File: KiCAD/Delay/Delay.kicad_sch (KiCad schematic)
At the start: 65 parts, among them J1 IN, J2 OUT, J3 Conn_01x03, J4 Conn_01x03, U1 TL072, U2 TL072, U3 PT2399, U4 L7805

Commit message: Delay PCB
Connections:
- net DELAY: now also R3.1; no longer R3.2
- net at C2.1, R6.2, U1.1: now also R8.2; no longer R8.1
- net at C3.2, R4.1, U1.6 (-): now also R2.1, R3.2; no longer R2.2, R3.1
- net at D1.2 (A), D3.1 (K), R9.1: now also R8.1; no longer R8.2
- net at C1.1, R1.1: now also R2.2; no longer R2.1
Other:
- moved on the sheet: R2, R3, R8
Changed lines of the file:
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@@
 	(symbol
 		(lib_id "HackSynth:R")
-		(at 62.23 78.74 90)
+		(at 62.23 78.74 270)
 		(unit 1)
 		(exclude_from_sim no)
@@
 		)
 		(property "Footprint" "HackSynth:R_Vertical_P2.54mm"
-			(at 62.23 80.518 90)
+			(at 62.23 76.962 90)
 			(effects
 				(font
@@
 	(symbol
 		(lib_id "HackSynth:R")
-		(at 81.28 49.53 90)
+		(at 81.28 49.53 270)
 		(unit 1)
 		(exclude_from_sim no)
@@
 		)
 		(property "Footprint" "HackSynth:R_Vertical_P2.54mm"
-			(at 81.28 51.308 90)
+			(at 81.28 47.752 90)
 			(effects
 				(font
@@
 	(symbol
 		(lib_id "HackSynth:R")
-		(at 43.18 99.06 90)
+		(at 43.18 99.06 270)
 		(unit 1)
 		(exclude_from_sim no)
@@
 		(dnp no)
 		(property "Reference" "R2"
-			(at 43.18 97.028 90)
+			(at 43.18 96.774 90)
 			(effects
 				(font
@@
 		)
 		(property "Footprint" "HackSynth:R_Vertical_P2.54mm"
-			(at 43.18 100.838 90)
+			(at 43.18 97.282 90)
 			(effects
 				(font

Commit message: Delay PCB
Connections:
- net at C21.2, R19.2, R23.2: now also R18.1; no longer R18.2
- net at C17.1, U3.16 (LPF1-IN): now also R18.2; no longer R18.1
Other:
- moved on the sheet: R18
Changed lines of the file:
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@@
 			"gtJqHJTWHJSWgtJqHJTWHJSWgtJqHJTWHJSWgtJqHJTWHJSWIpK2hxHREqNQWjNQWoq1tJcDEW2x"
 			"j38zCAGlpVhLiyAaBqWloLSIF/HOJ7z9UadpjtIi3kM6v9Ov2xhL/v/mElWvvu6fRQAAAABJRU5E"
-			"rkJggg=="
+			"rkJgggAgACAAIAAgACAAIAAgAD0AIAAiAHMAdABhAHQAaQBjAHQAZQB4AHQAIgANAA0ACgAvAD4A"
+			"DQANAAoAPAAvAGkAZgA+AA0ADQAKADwAaQBmACAAaQBkAD0AIgBhAHQAbwBtACgARgBvAG8AdABu"
+			"AG8AdABlAFQAZQB4AHQATABpAG4AawApACIAPgANAA0ACgA8AGMAYwBzAHkAcwBsAGkAbgBrAA0A"
+			"DQAKAGYAbwBuAHQAIAAgACAAIAAgACAAIAAgACAAIAAgACAAIAAgACAAIAA9ACAAIgBnAHQAZgAo"
+			"AFQAYQBzAGsARABpAGEAbABvAGcAUwB0AHkAbABlACwAIAAxADUALAAgADAAKQAiAA0ADQAKAGYA"
+			"bwByAGUAZwByAG8AdQBuAGQAIAAgACAAIAAgACAAIAAgACAAIAA9ACAAIgBnAHQAYwAoAFQAYQBz"
+			"AGsARABpAGEAbABvAGcAUwB0AHkAbABlACwAIAAxADUALAAgADAALAAgADMAOAAwADMAKQAiAA0A"
+			"DQAKAC8APgANAA0ACgA8AC8AaQBmAD4ADQANAAoAPABpAGYAIABpAGQAPQAiAGEAdABvAG0AKABF"
+			"AHgAcABhAG4AZABlAGQARgBvAG8AdABlAHIAQQByAGUAYQApACIAPgANAA0ACgA8AGUAbABlAG0A"
+			"ZQBuAHQADQANAAoAYgBhAGMAawBnAHIAbwB1AG4AZAAgACAAIAAgACAAIAAgACAAIAAgAD0AIAAi"
+			"AHQAaABlAG0AZQBhAGIAbABlACgAZAB0AGIAKABUAGEAcwBrAEQAaQBhAGwAbwBnACwAIAAxADUA"
+			"LAAgADAAKQAsACAAdABoAHIAZQBlAGQAZgBhAGMAZQApACIADQANAAoAcABhAGQAZABpAG4AZwAg"
+			"ACAAIAAgACAAIAAgACAAIAAgACAAIAAgAD0AIAAiAHQAaABlAG0AZQBhAGIAbABlACgAZwB0AG0A"
+			"YQByACgAVABhAHMAawBEAGkAYQBsAG8AZwAsACAAMQA4ACwAIAAwACwAIAAzADYAMAAyACkALABy"
+			"AGUAYwB0ACgAMQAwAHIAcAAsADAALAAxADAAcgBwACwANQByAHAAKQApACIADQANAAoALwA+AA0A"
+			"DQAKADwALwBpAGYAPgANAA0ACgA8AGkAZgAgAGkAZAA9ACIAYQB0AG8AbQAoAEUAeABwAGEAbgBk"
+			"AGUAZABGAG8AbwB0AGUAcgBUAGUAeAB0ACkAIgA+AA0ADQAKADwAZQBsAGUAbQBlAG4AdAANAA0A"
+			"CgBmAG8AbgB0ACAAIAAgACAAIAAgACAAIAAgACAAIAAgACAAIAAgACAAPQAgACIAZwB0AGYAKABU"
+			"AGEAcw=="
 		)
 	)
@@
 	(symbol
 		(lib_id "HackSynth:R")
-		(at 251.46 95.25 90)
+		(at 251.46 95.25 270)
 		(unit 1)
 		(exclude_from_sim no)
@@
 		)
 		(property "Footprint" "HackSynth:R_Vertical_P2.54mm"
-			(at 251.46 97.028 90)
+			(at 251.46 93.472 90)
 			(effects
 				(font

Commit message: Backup Cleanup
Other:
- moved on the sheet: C6, J3, J4, R24, R25, RV3

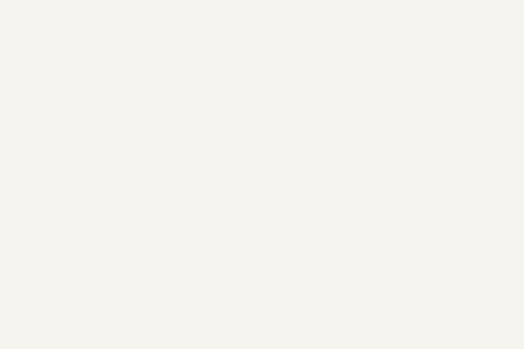
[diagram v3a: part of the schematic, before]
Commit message: Footprint Edits
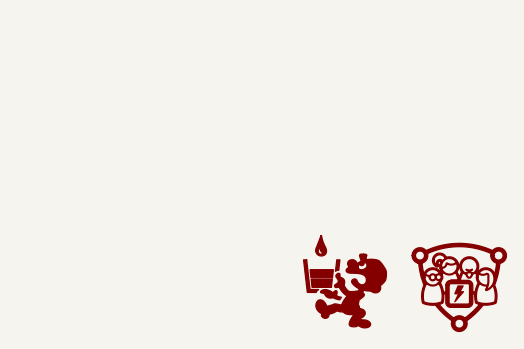
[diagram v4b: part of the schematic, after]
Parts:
- added G1: ~, symbol HackSynth:CCHS_Logo
- added G2: ~, symbol HackSynth:Logo_PancakeLegend
- C13: footprint HackSynth:CP_Radial_D5.2mm_P2.50mm_LayDown -> HackSynth:CP_Radial_D5.2mm_P2.50mm_LayDown_Mirror
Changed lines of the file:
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@@
 	)
 	(symbol
+		(lib_id "HackSynth:CCHS_Logo")
+		(at 275.59 172.72 0)
+		(unit 1)
+		(exclude_from_sim no)
+		(in_bom yes)
+		(on_board yes)
+		(dnp no)
+		(fields_autoplaced yes)
+		(property "Reference" "G1"
+			(at 275.59 180.34 0)
+			(effects
+				(font
+					(size 1.27 1.27)
+				)
+				(hide yes)
+			)
+		)
+		(property "Value" "~"
+			(at 281.94 173.89 0)
+			(effects
+				(font
+					(size 1.27 1.27)
+				)
+				(justify left)
+			)
+		)
+		(property "Footprint" ""
+			(at 275.59 172.72 0)
+			(effects
+				(font
+					(size 1.27 1.27)
+				)
+				(hide yes)
+			)
+		)
+		(property "Datasheet" ""
+			(at 275.59 172.72 0)
+			(effects
+				(font
+					(size 1.27 1.27)
+				)
+				(hide yes)
+			)
+		)
+		(property "Description" ""
+			(at 275.59 172.72 0)
+			(effects
+				(font
+					(size 1.27 1.27)
+				)
+				(hide yes)
+			)
+		)
+		(instances
+			(project ""
+				(path "/2ec94028-47e2-4676-a4ba-5453efde3459"
+					(reference "G1")
+					(unit 1)
+				)
+			)
+		)
+	)
+	(symbol
 		(lib_id "Device:C")
 		(at 245.11 111.76 0)
@@
 	)
 	(symbol
+		(lib_id "HackSynth:Logo_PancakeLegend")
+		(at 262.89 173.355 0)
+		(unit 1)
+		(exclude_from_sim no)
+		(in_bom yes)
+		(on_board yes)
+		(dnp no)
+		(fields_autoplaced yes)
+		(property "Reference" "G2"
+			(at 262.89 180.975 0)
+			(effects
+				(font
+					(size 1.27 1.27)
+				)
+				(hide yes)
+			)
+		)
+		(property "Value" "~"
+			(at 269.24 173.2549 0)
+			(effects
+				(font
+					(size 1.27 1.27)
+				)
+				(justify left)
+			)
+		)
+		(property "Footprint" ""
+			(at 262.89 173.355 0)
+			(effects
+				(font
+					(size 1.27 1.27)
+				)
+				(hide yes)
+			)
+		)
+		(property "Datasheet" ""
+			(at 262.89 173.355 0)
+			(effects
+				(font
+					(size 1.27 1.27)
+				)
+				(hide yes)
+			)
+		)
+		(property "Description" ""
+			(at 262.89 173.355 0)
+			(effects
+				(font
+					(size 1.27 1.27)
+				)
+				(hide yes)
+			)
+		)
+		(instances
+			(project ""
+				(path "/2ec94028-47e2-4676-a4ba-5453efde3459"
+					(reference "G2")
+					(unit 1)
+				)
+			)
+		)
+	)
+	(symbol
 		(lib_id "power:VDD")
 		(at 39.37 132.08 0)
@@
 			)
 		)
-		(property "Footprint" "HackSynth:CP_Radial_D5.2mm_P2.50mm_LayDown"
+		(property "Footprint" "HackSynth:CP_Radial_D5.2mm_P2.50mm_LayDown_Mirror"
 			(at 193.04 98.7552 0)
 			(effects
